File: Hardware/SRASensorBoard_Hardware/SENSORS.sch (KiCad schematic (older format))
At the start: 23 parts

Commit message: Sciency stuff for the board
finished!
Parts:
- removed Conn?: Molex_SL_04, MRDT_Connectors:MOLEX_SL_04_Vertical, symbol MRDT_Connectors:Molex_SL_04
- added Conn? (x4): Molex_SL_04, MRDT_Connectors:MOLEX_SL_04_Vertical, symbol MRDT_Connectors:Molex_SL_04
- added D? (x12): LED, Diode_SMD:D_0603_1608Metric_Pad1.05x0.95mm_HandSolder, symbol Device:LED
- added Q? (x2): BSS138, Package_TO_SOT_SMD:SOT-23, symbol Transistor_FET:BSS138
- added R? (x4): 10K, Resistor_SMD:R_0603_1608Metric_Pad1.05x0.95mm_HandSolder, symbol Device:R
- added R? (x12): 330, Resistor_SMD:R_0603_1608Metric_Pad1.05x0.95mm_HandSolder, symbol Device:R
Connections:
- net +3V3: now also Conn?.1, Conn?.1, Q?.1 (G), Q?.1 (G), R?.1, R?.1
- net +5V: now also Conn?.1
- net GND: now also J?.5 (Shield), Conn?.2, Conn?.2, Conn?.2, Conn?.2, D?.1 (K), D?.1 (K), D?.1 (K), D?.1 (K), D?.1 (K), D?.1 (K), D?.1 (K), D?.1 (K), D?.1 (K), D?.1 (K), D?.1 (K), D?.1 (K)
- net O2_RX: now also R?.1
- net O2_TX: now also R?.1
- net TIVA_USB_RX: now also R?.1
- net TIVA_USB_TX: now also R?.1
- new net: D?.2 (A), R?.2 (x12)
- new net +12V: Conn?.1, R?.1, R?.1
- new net CO2_RX: Conn?.4, R?.1
- new net CO2_TX: Conn?.3, R?.1
- new net N2O_RX: Conn?.4, Q?.2 (S), Q?.3 (D), R?.1, R?.2, R?.2
- new net N2O_TX: Conn?.3, Q?.2 (S), Q?.3 (D), R?.1, R?.2, R?.2
- new net NO2_RX: Conn?.4, R?.1
- new net NO2_TX: Conn?.3, R?.1
- new net NO_RX: Conn?.4, R?.1
- new net NO_TX: Conn?.3, R?.1
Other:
- note added: "N2O_Sensor\n"
- note added: "NO2_Sensor\n"
- note added: "NO_Sensor"
- note added: "PINK"
- note added: "PINK\n"
- moved on the sheet: C?, Conn?, J?, Q?, R?, U?

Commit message: Science_sensor reveiw 1
Yep
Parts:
- J1: renamed from J?; footprint custom:292303-1 -> Connector_USB:USB_A_Stewart_SS-52100-001_Horizontal
- gave numbers to parts that had none: 55
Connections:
- net NO_RX renamed NO_SDA
- net NO_TX renamed NO_SCL
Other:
- note added: "0.22A"
- note added: "50V\n"

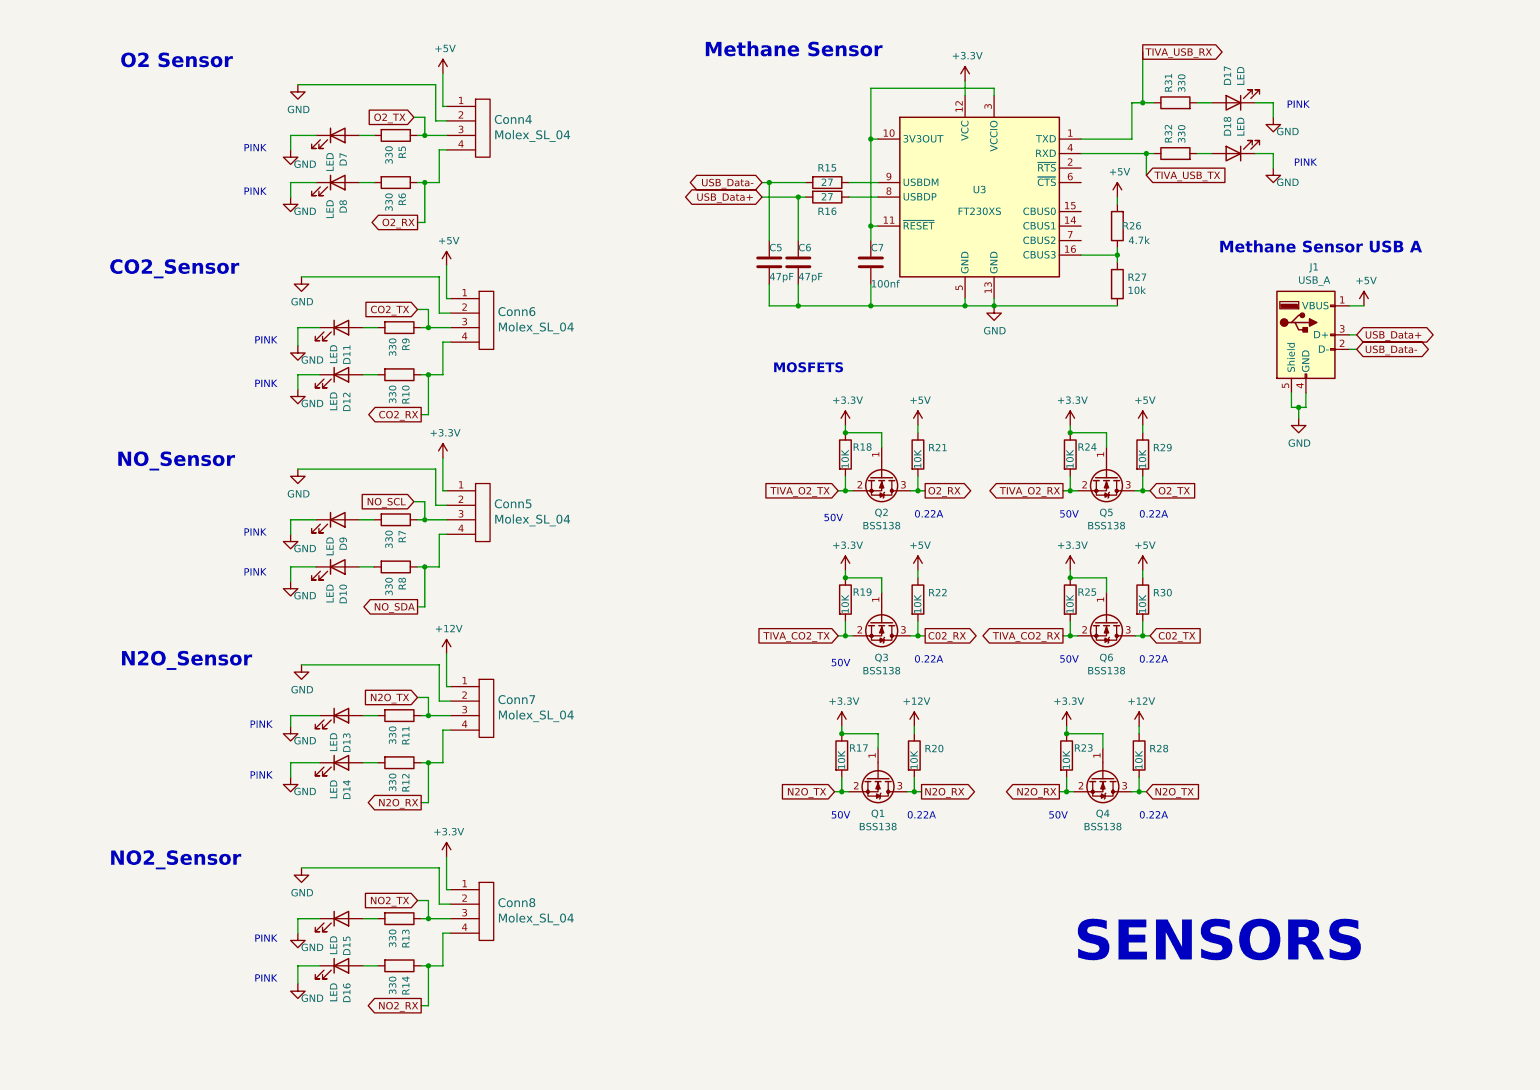
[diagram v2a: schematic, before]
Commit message: Layout started, edge cut fix
ladybug is not pleased
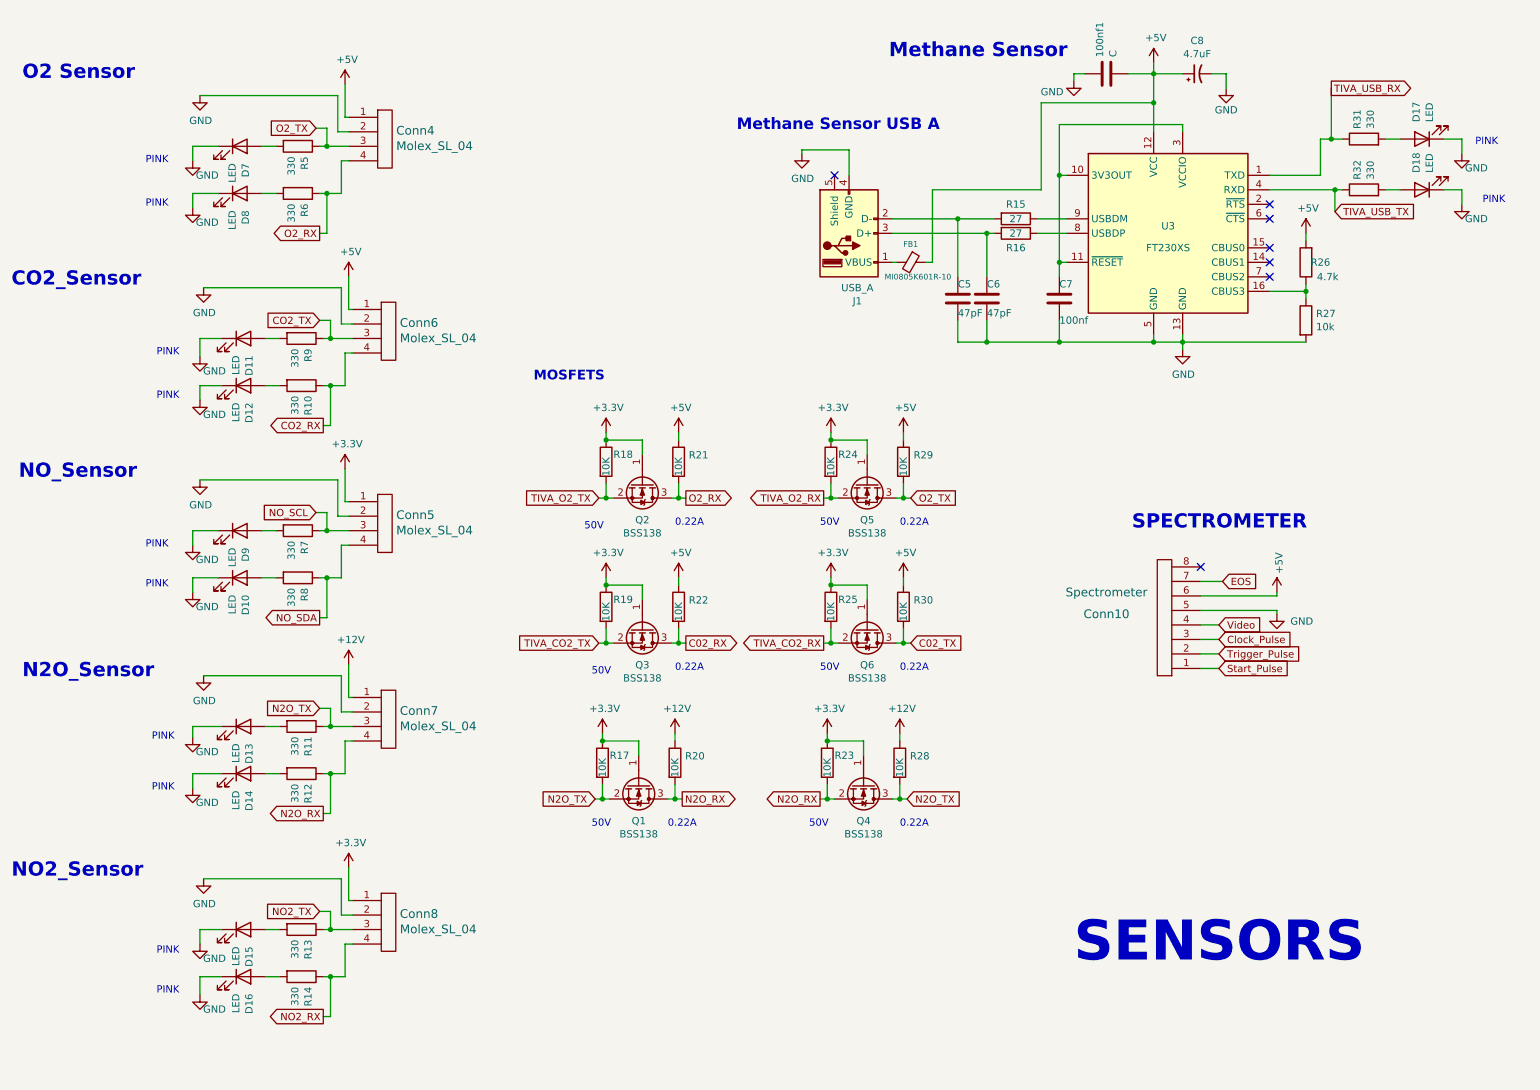
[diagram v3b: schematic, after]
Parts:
- added 100nf1: C, Capacitor_SMD:C_0603_1608Metric_Pad1.05x0.95mm_HandSolder, symbol Device:C
- added C8: 4.7uF, Capacitor_THT:CP_Radial_D12.5mm_P2.50mm, symbol Device:CP1_Small
- added Conn10: Spectrometer, MRDT_Connectors:MOLEX_SL_08_Vertical, symbol MRDT_Connectors:Molex_SL_08
- added FB1: MI0805K601R-10, Resistor_SMD:R_0805_2012Metric_Pad1.15x1.40mm_HandSolder, symbol Device:Ferrite_Bead_Small
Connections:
- net +3V3: no longer U3.12 (VCC)
- net +5V: now also U3.12 (VCC), 100nf1.2, C8.1, Conn10.6, FB1.1; no longer J1.1 (VBUS)
- net GND: now also 100nf1.1, C8.2, Conn10.5; no longer J1.5 (Shield)
- net USB_Data+: no longer names the net of C6.1, J1.3 (D+), R16.2
- net USB_Data-: no longer names the net of C5.1, J1.2 (D-), R15.2
- new net: FB1.2, J1.1 (VBUS)
- new net Clock_Pulse: Conn10.3
- new net EOS: Conn10.7
- new net Start_Pulse: Conn10.1
- new net Trigger_Pulse: Conn10.2
- new net Video: Conn10.4
- no-connect marks 0 -> 7
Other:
- note added: "SPECTROMETER"
- moved on the sheet: C5, C6, C7, Conn4, Conn5, Conn6, Conn7, Conn8, D10, D11, D12, D13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

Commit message: Broad Progress 2-oof
Pre-oops need to add 6 mosfets for spectrometer
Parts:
- C8: footprint Capacitor_THT:CP_Radial_D12.5mm_P2.50mm -> Capacitor_THT:CP_Radial_D12.5mm_P5.00mm
- C9: renamed from 100nf1; value C -> 100nf
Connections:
- net N2O_RX: no longer Q4.2 (S), R23.2
- net N2O_TX: no longer Q1.2 (S), R17.2
- new net TIVA_N2O_RX: Q4.2 (S), R23.2
- new net TIVA_N2O_TX: Q1.2 (S), R17.2
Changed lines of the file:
@@
 $EndComp
 Text GLabel 4850 5850 0    50   Input ~ 0
-N2O_TX
+TIVA_N2O_TX
 Text GLabel 5450 5850 2    50   Output ~ 0
 N2O_RX
@@
 N2O_TX
 Text GLabel 6400 5850 0    50   Output ~ 0
-N2O_RX
+TIVA_N2O_RX
 $Comp
 L Device:LED D?
@@
 $EndComp
 $Comp
-L Device:C 100nf1
+L Device:C C9
 U 1 1 5FDA3C36
 P 8375 850
-F 0 "100nf1" H 8490 896 50  0000 L CNN
-F 1 "C" H 8490 805 50  0000 L CNN
+F 0 "C9" H 8490 896 50  0000 L CNN
+F 1 "100nf" H 8490 805 50  0000 L CNN
 F 2 "Capacitor_SMD:C_0603_1608Metric_Pad1.05x0.95mm_HandSolder" H 8413 700 50  0001 C CNN
 F 3 "~" H 8375 850 50  0001 C CNN
@@
 F 0 "C8" V 9228 850 50  0000 C CNN
 F 1 "4.7uF" V 9137 850 50  0000 C CNN
-F 2 "Capacitor_THT:CP_Radial_D12.5mm_P2.50mm" H 9000 850 50  0001 C CNN
+F 2 "Capacitor_THT:CP_Radial_D12.5mm_P5.00mm" H 9000 850 50  0001 C CNN
 F 3 "~" H 9000 850 50  0001 C CNN
 	1    9000 850

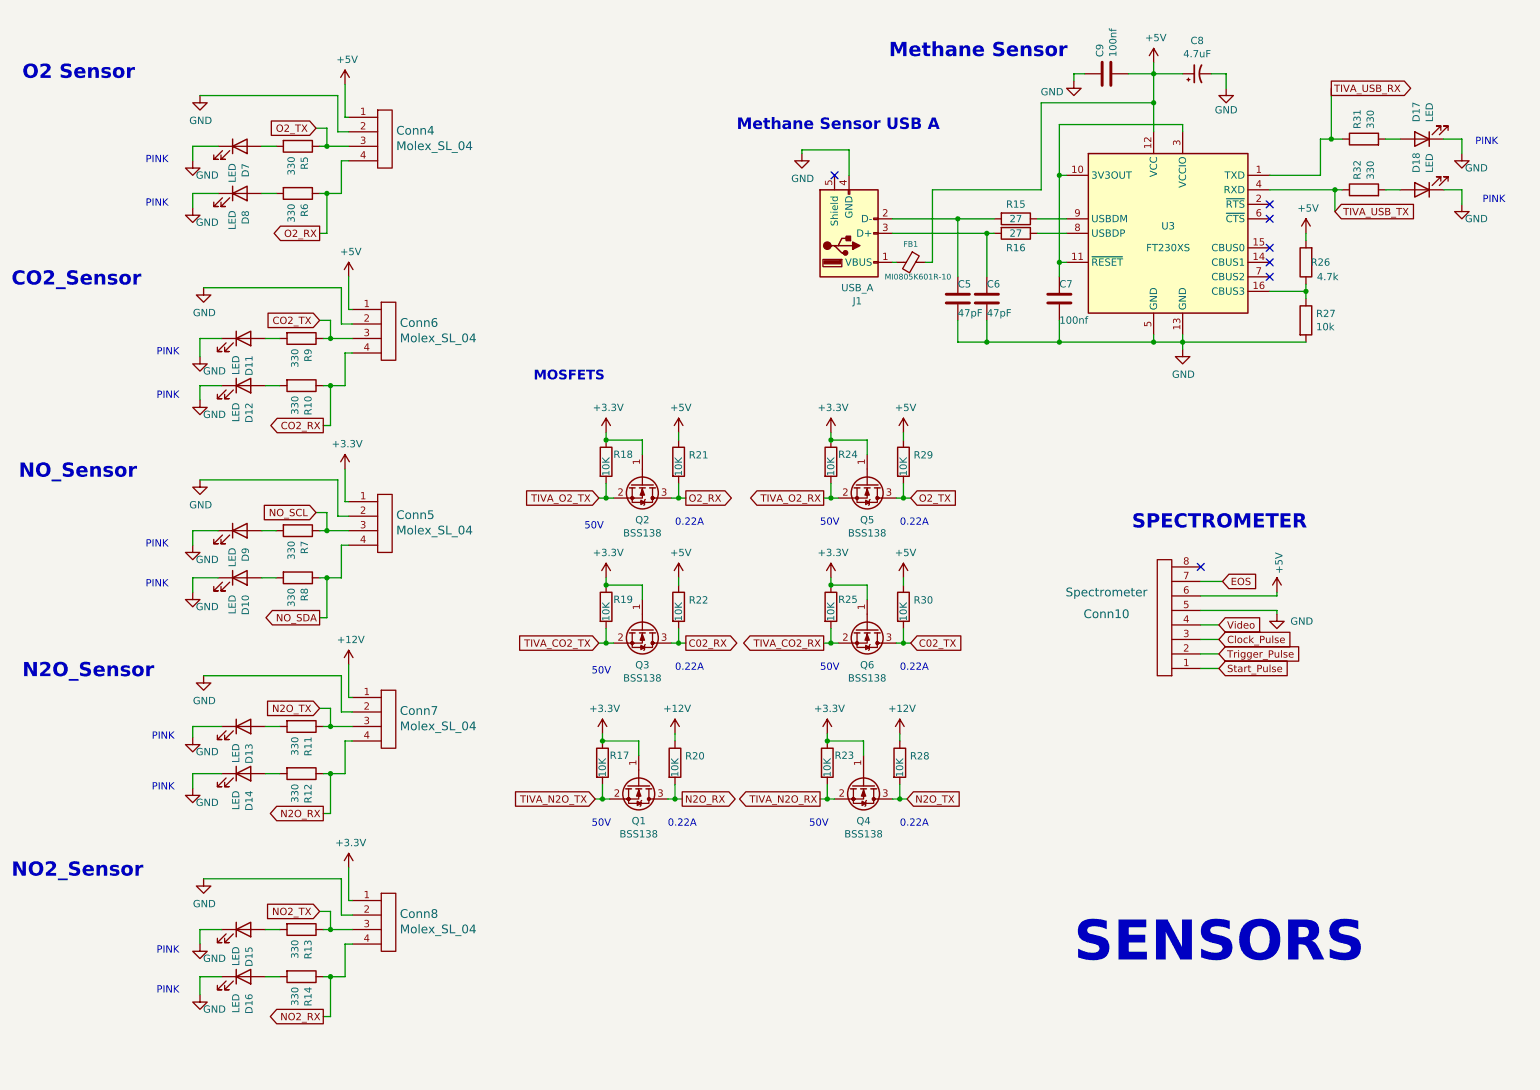
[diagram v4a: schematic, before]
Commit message: Board Progress 3
New mosfets are in but old mosfets need some clean up
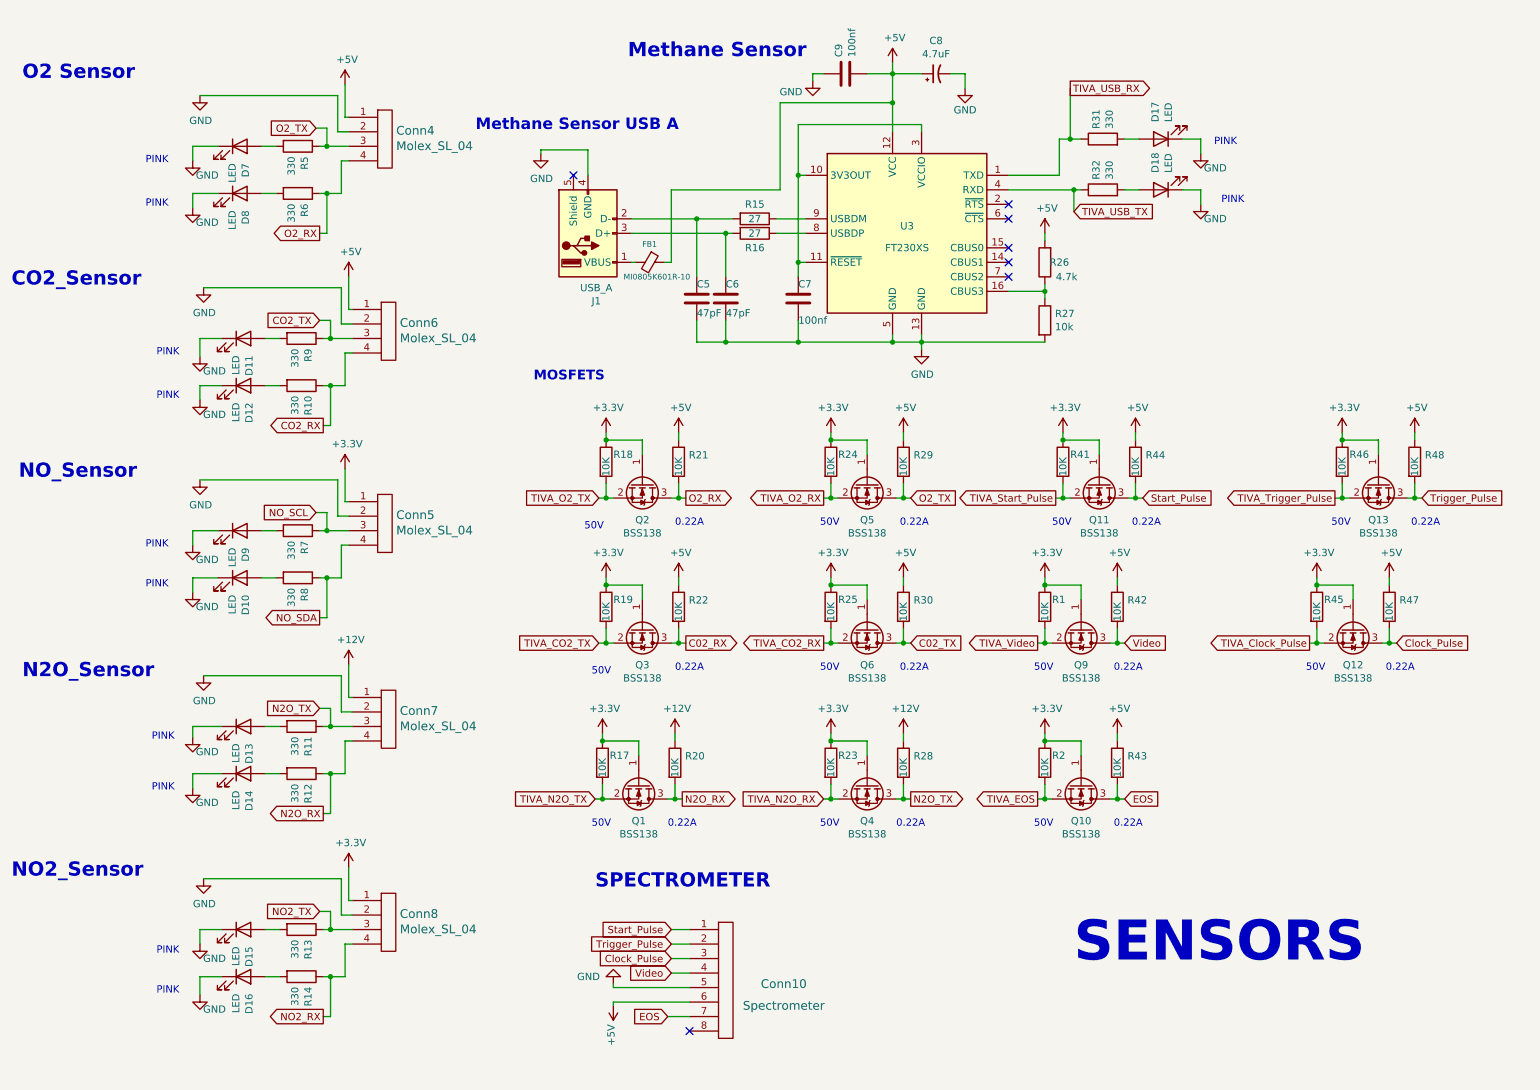
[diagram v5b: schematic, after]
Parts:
- added Q10, Q11, Q12, Q13, Q9: BSS138, Package_TO_SOT_SMD:SOT-23, symbol Transistor_FET:BSS138
- added R1, R2, R41, R42, R43, R44, R45, R46, R47, R48: 10K, Resistor_SMD:R_0603_1608Metric_Pad1.05x0.95mm_HandSolder, symbol Device:R
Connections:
- net +3V3: now also Q10.1 (G), Q11.1 (G), Q12.1 (G), Q13.1 (G), Q9.1 (G), R1.1, R2.1, R41.1, R45.1, R46.1
- net +5V: now also R42.1, R43.1, R44.1, R47.1, R48.1
- net Clock_Pulse: now also Q12.3 (D), R47.2
- net EOS: now also Q10.3 (D), R43.2
- net Start_Pulse: now also Q11.3 (D), R44.2
- net Trigger_Pulse: now also Q13.3 (D), R48.2
- net Video: now also Q9.3 (D), R42.2
- new net TIVA_Clock_Pulse: Q12.2 (S), R45.2
- new net TIVA_EOS: Q10.2 (S), R2.2
- new net TIVA_Start_Pulse: Q11.2 (S), R41.2
- new net TIVA_Trigger_Pulse: Q13.2 (S), R46.2
- new net TIVA_Video: Q9.2 (S), R1.2
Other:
- moved on the sheet: C5, C6, C7, C8, C9, Conn10, D17, D18, FB1, J1, R15, R16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

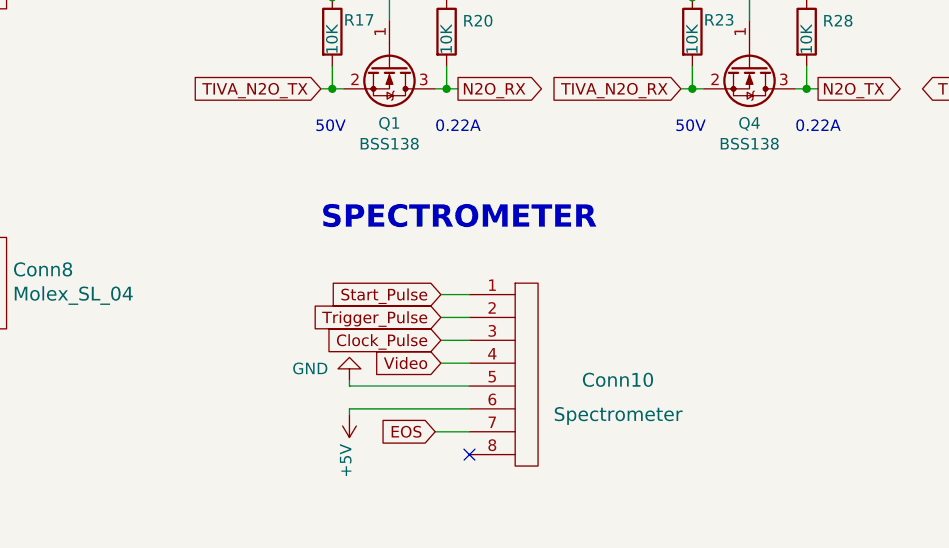
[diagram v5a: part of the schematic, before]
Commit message: Board Progress 6 (Post Review)
Finished moving vias off pads and labeling most things and added leds for spectrometer
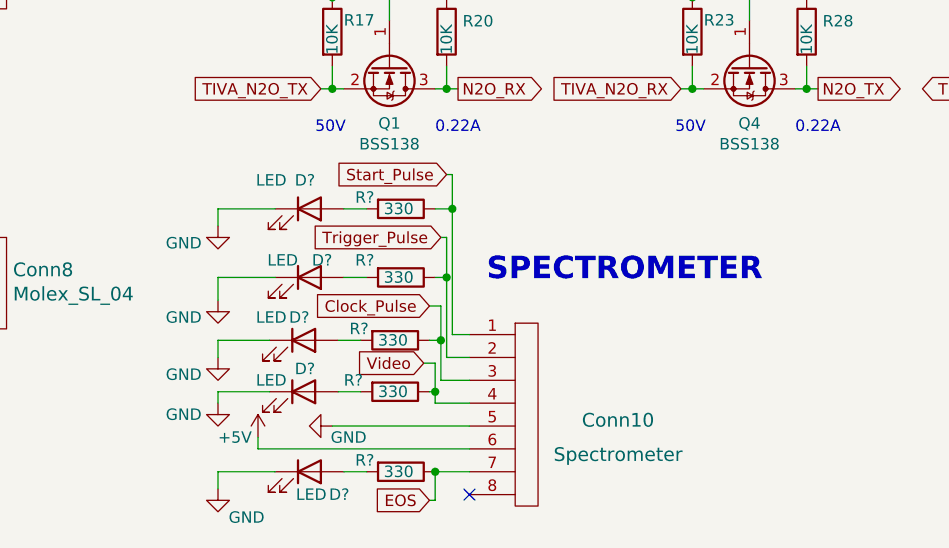
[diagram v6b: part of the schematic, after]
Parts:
- added D? (x5): LED, Diode_SMD:D_0603_1608Metric_Pad1.05x0.95mm_HandSolder, symbol Device:LED
- added R? (x5): 330, Resistor_SMD:R_0603_1608Metric_Pad1.05x0.95mm_HandSolder, symbol Device:R
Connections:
- net Clock_Pulse: now also R?.1
- net EOS: now also R?.1
- net GND: now also D?.1 (K), D?.1 (K), D?.1 (K), D?.1 (K), D?.1 (K)
- net Start_Pulse: now also R?.1
- net Trigger_Pulse: now also R?.1
- net Video: now also R?.1
- new net: D?.2 (A), R?.2 (x5)
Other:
- moved on the sheet: Conn10

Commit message: Board Progress 7 (final rev 1)
Final edits for REV 1
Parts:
- removed D? (x5): LED, Diode_SMD:D_0603_1608Metric_Pad1.05x0.95mm_HandSolder, symbol Device:LED
- removed R? (x5): 330, Resistor_SMD:R_0603_1608Metric_Pad1.05x0.95mm_HandSolder, symbol Device:R
- C8: footprint Capacitor_THT:CP_Radial_D12.5mm_P5.00mm -> Capacitor_THT:CP_Radial_D5.0mm_P2.50mm
